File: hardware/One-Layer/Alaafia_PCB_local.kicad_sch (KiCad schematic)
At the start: 6 parts, among them J1 BATTERY, U1 ESP32-C3_SUPERMINI_TH, U2 BMI160, U3 MT3608

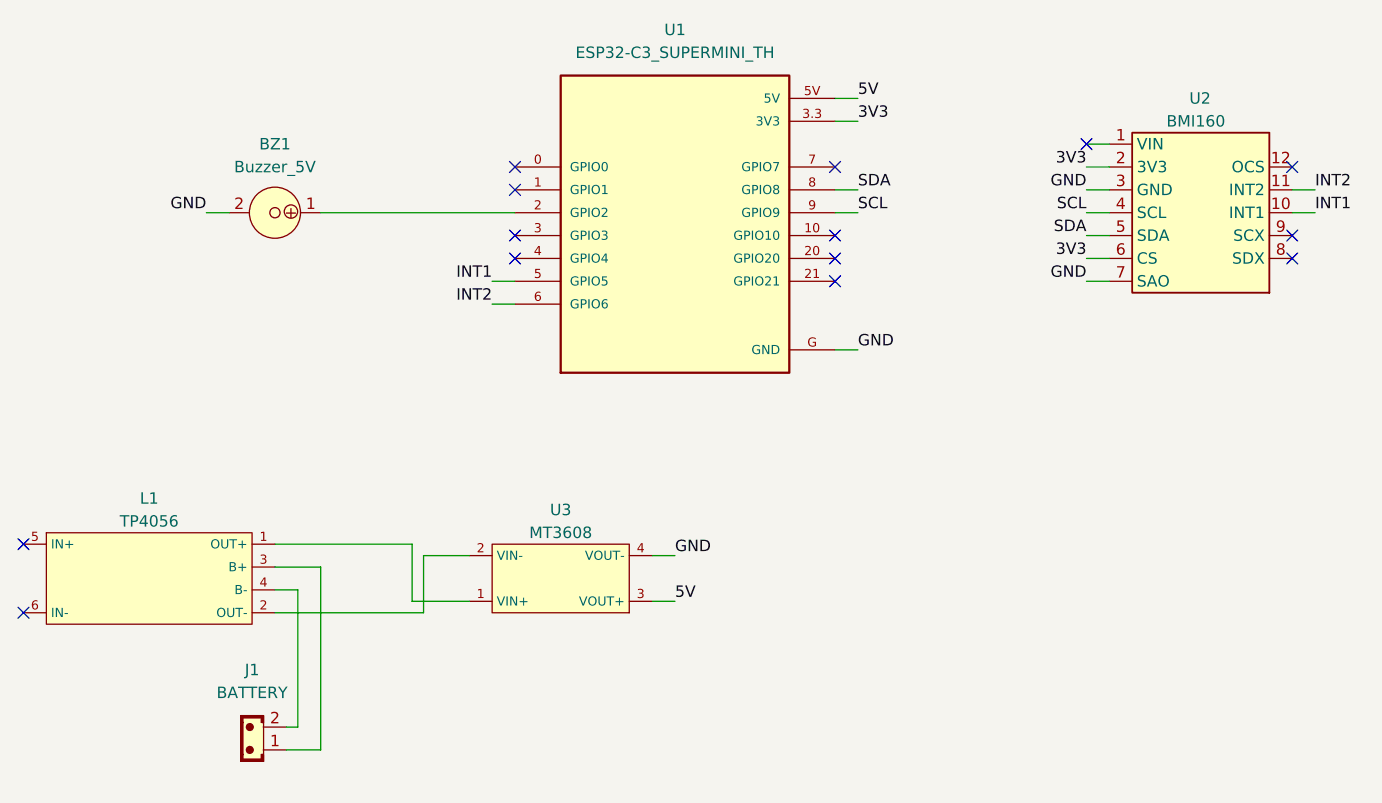
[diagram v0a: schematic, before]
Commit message: Local PCB with button and SIM JST
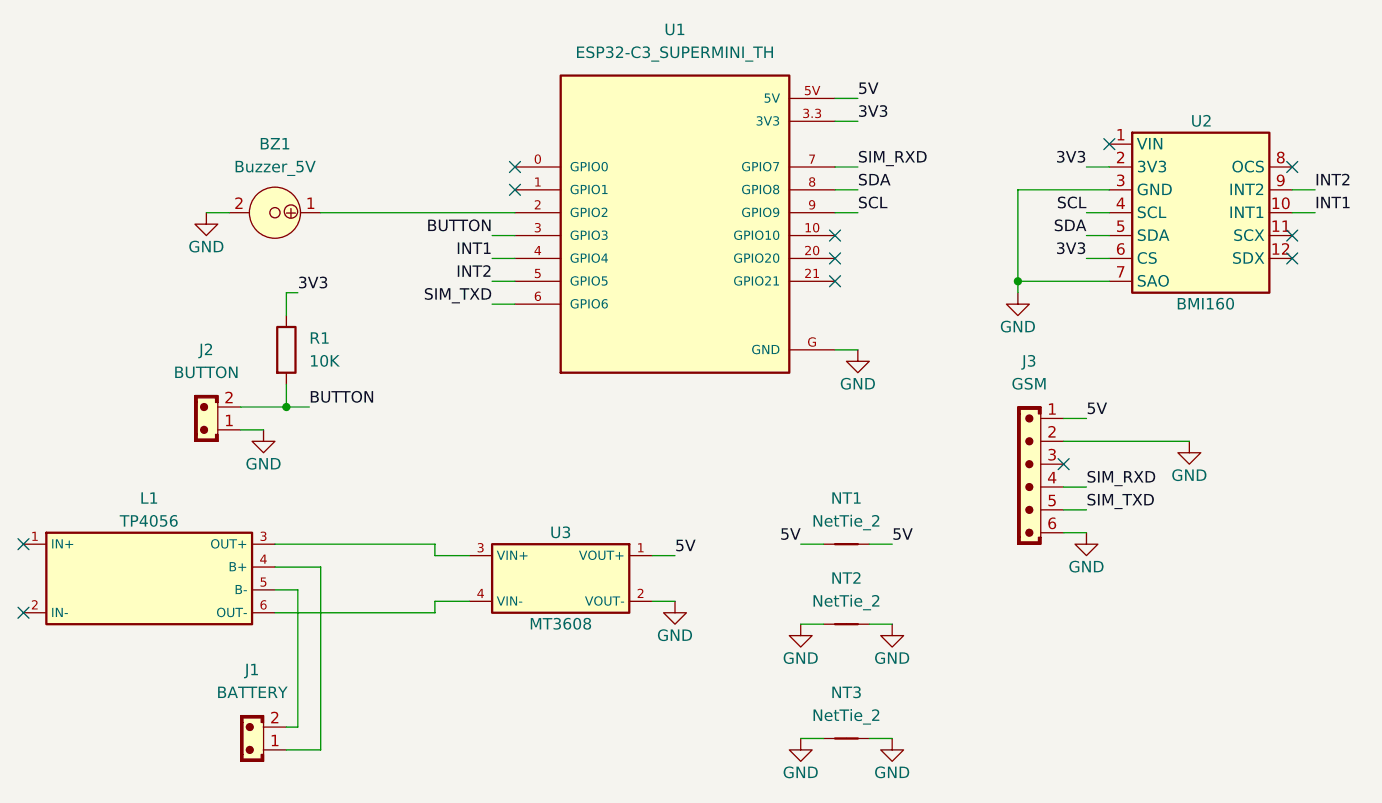
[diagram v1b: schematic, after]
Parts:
- added J2: BUTTON, Connector_JST:JST_EH_B2B-EH-A_1x02_P2.50mm_Vertical, symbol PCM_SL_Connectors:JST_02
- added J3: GSM, Connector_JST:JST_EH_B6B-EH-A_1x06_P2.50mm_Vertical, symbol PCM_SL_Connectors:JST_06
- added NT1, NT3: NetTie_2, PCM_SL_Jumpers:JUP_P5.08mm, symbol Device:NetTie_2
- added NT2: NetTie_2, PCM_SL_Jumpers:JUP_P14mm, symbol Device:NetTie_2
- added R1: 10K, Resistor_THT:R_Axial_DIN0411_L9.9mm_D3.6mm_P15.24mm_Horizontal, symbol Device:R
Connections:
- net 3V3: now also R1.1
- net 5V: now also U3.1 (VOUT+), J3.1, NT1.1, NT1.2; no longer U3.3 (VOUT+)
- net GND: now also U3.2 (VOUT-), J2.1, J3.2, J3.6, NT2.1, NT2.2, NT3.1, NT3.2; no longer U3.4 (VOUT-)
- net INT1: now also U1.4 (GPIO4); no longer U1.5 (GPIO5)
- net INT2: now also U1.5 (GPIO5), U2.9 (INT2); no longer U1.6 (GPIO6), U2.11 (INT2)
- net at J1.1: now also L1.4 (B+); no longer L1.3 (B+)
- net at J1.2: now also L1.5 (B-); no longer L1.4 (B-)
- net BUTTON: now reaches U1.3 (GPIO3)
- net BUTTON: now also J2.2, R1.2
- net SIM_RXD: now reaches U1.7 (GPIO7)
- net SIM_RXD: now also J3.4
- net at L1.1 (IN+): no longer U3.1 (VIN+)
- net at L1.2 (IN-): no longer U3.2 (VIN-)
- net at L1.6 (OUT-): now also U3.4 (VIN-)
- new net: L1.3 (OUT+), U3.3 (VIN+)
- new net SIM_TXD: J3.5, U1.6 (GPIO6)
- no-connect marks 14 -> 12
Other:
- moved on the sheet: U2, U3
